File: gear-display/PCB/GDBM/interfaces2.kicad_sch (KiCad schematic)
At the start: 1 part

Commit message: updates
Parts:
- added J?: Con_Screw_1x04_691313510004, KD_Connector_Screw:CON_508_1X04_691313510004_Mated, symbol KD_Connector_Screw:Con_Screw_1x04_691313510004
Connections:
- net +5V: now reaches J?.1 (Pin_1)
- net SDA: now reaches J?.2 (Pin_2)
- net SCL: now reaches J?.3 (Pin_3)
- net GND: now reaches J?.4 (Pin_4)
- net GND: now also J?.4 (Pin_4)
- new net +12V: J?.1 (Pin_1)
- new net PWM: J?.2 (Pin_2)
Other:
- moved on the sheet: J?
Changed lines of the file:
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@@
 (kicad_sch (version 20211123) (generator eeschema)
   (paper "A4")
-  (symbol (lib_id "KD_Connector_Screw:Con_Screw_1x04_691313510004") (at 166.37 53.34 0) (unit 1)
+  (bus_entry (at 163.83 58.42) (size 2.54 2.54)
+    (stroke (width 0) (type default) (color 0 0 0 0))
+  )
+  (bus_entry (at 163.83 60.96) (size 2.54 2.54)
+    (stroke (width 0) (type default) (color 0 0 0 0))
+  )
+  (wire (pts (xy 184.15 58.42) (xy 181.61 58.42))
+    (stroke (width 0) (type default) (color 0 0 0 0))
+  )
+  (bus (pts (xy 163.83 58.42) (xy 163.83 60.96))
+    (stroke (width 0) (type default) (color 0 0 0 0))
+  )
+  (wire (pts (xy 181.61 54.61) (xy 181.61 58.42))
+    (stroke (width 0) (type default) (color 0 0 0 0))
+  )
+  (wire (pts (xy 175.26 92.71) (xy 180.34 92.71))
+    (stroke (width 0) (type default) (color 0 0 0 0))
+  )
+  (wire (pts (xy 163.83 95.25) (xy 180.34 95.25))
+    (stroke (width 0) (type default) (color 0 0 0 0))
+  )
+  (bus (pts (xy 163.83 60.96) (xy 163.83 64.77))
+    (stroke (width 0) (type default) (color 0 0 0 0))
+  )
+  (wire (pts (xy 166.37 63.5) (xy 184.15 63.5))
+    (stroke (width 0) (type default) (color 0 0 0 0))
+  )
+  (wire (pts (xy 180.34 100.33) (xy 175.26 100.33))
+    (stroke (width 0) (type default) (color 0 0 0 0))
+  )
+  (wire (pts (xy 166.37 60.96) (xy 184.15 60.96))
+    (stroke (width 0) (type default) (color 0 0 0 0))
+  )
+  (wire (pts (xy 175.26 100.33) (xy 175.26 104.14))
+    (stroke (width 0) (type default) (color 0 0 0 0))
+  )
+  (wire (pts (xy 175.26 90.17) (xy 175.26 92.71))
+    (stroke (width 0) (type default) (color 0 0 0 0))
+  )
+  (wire (pts (xy 175.26 97.79) (xy 180.34 97.79))
+    (stroke (width 0) (type default) (color 0 0 0 0))
+  )
+  (wire (pts (xy 181.61 66.04) (xy 181.61 68.58))
+    (stroke (width 0) (type default) (color 0 0 0 0))
+  )
+  (bus (pts (xy 163.83 55.88) (xy 163.83 58.42))
+    (stroke (width 0) (type default) (color 0 0 0 0))
+  )
+  (wire (pts (xy 184.15 66.04) (xy 181.61 66.04))
+    (stroke (width 0) (type default) (color 0 0 0 0))
+  )
+  (bus (pts (xy 158.75 55.88) (xy 163.83 55.88))
+    (stroke (width 0) (type default) (color 0 0 0 0))
+  )
+  (label "SCL" (at 167.64 63.5 0)
+    (effects (font (size 1.27 1.27)) (justify left bottom))
+  )
+  (label "SDA" (at 167.64 60.96 0)
+    (effects (font (size 1.27 1.27)) (justify left bottom))
+  )
+  (hierarchical_label "PWM" (shape input) (at 163.83 95.25 180)
+    (effects (font (size 1.27 1.27)) (justify right))
+  )
+  (hierarchical_label "I2C" (shape input) (at 158.75 55.88 180)
+    (effects (font (size 1.27 1.27)) (justify right))
+  )
+  (symbol (lib_id "power:+12V") (at 175.26 90.17 0) (unit 1)
     (in_bom yes) (on_board yes) (fields_autoplaced)
-    (property "Reference" "J?" (id 0) (at 173.99 55.8799 0)
+    (property "Reference" "#PWR?" (id 0) (at 175.26 93.98 0)
+      (effects (font (size 1.27 1.27)) hide)
+    )
+    (property "Value" "+12V" (id 1) (at 175.26 85.09 0))
+    (property "Footprint" "" (id 2) (at 175.26 90.17 0)
+      (effects (font (size 1.27 1.27)) hide)
+    )
+    (property "Datasheet" "" (id 3) (at 175.26 90.17 0)
+      (effects (font (size 1.27 1.27)) hide)
+    )
+    (pin "1")
+  )
+  (symbol (lib_id "power:GND") (at 175.26 104.14 0) (mirror y) (unit 1)
+    (in_bom yes) (on_board yes)
+    (property "Reference" "#PWR?" (id 0) (at 175.26 110.49 0)
+      (effects (font (size 1.27 1.27)) hide)
+    )
+    (property "Value" "GND" (id 1) (at 175.26 107.95 0))
+    (property "Footprint" "" (id 2) (at 175.26 104.14 0)
+      (effects (font (size 1.27 1.27)) hide)
+    )
+    (property "Datasheet" "" (id 3) (at 175.26 104.14 0)
+      (effects (font (size 1.27 1.27)) hide)
+    )
+    (pin "1")
+  )
+  (symbol (lib_id "power:GND") (at 181.61 68.58 0) (mirror y) (unit 1)
+    (in_bom yes) (on_board yes)
+    (property "Reference" "#PWR?" (id 0) (at 181.61 74.93 0)
+      (effects (font (size 1.27 1.27)) hide)
+    )
+    (property "Value" "GND" (id 1) (at 181.61 72.39 0))
+    (property "Footprint" "" (id 2) (at 181.61 68.58 0)
+      (effects (font (size 1.27 1.27)) hide)
+    )
+    (property "Datasheet" "" (id 3) (at 181.61 68.58 0)
+      (effects (font (size 1.27 1.27)) hide)
+    )
+    (pin "1")
+  )
+  (symbol (lib_id "power:+5V") (at 181.61 54.61 0) (unit 1)
+    (in_bom yes) (on_board yes) (fields_autoplaced)
+    (property "Reference" "#PWR?" (id 0) (at 181.61 58.42 0)
+      (effects (font (size 1.27 1.27)) hide)
+    )
+    (property "Value" "+5V" (id 1) (at 181.61 49.53 0))
+    (property "Footprint" "" (id 2) (at 181.61 54.61 0)
+      (effects (font (size 1.27 1.27)) hide)
+    )
+    (property "Datasheet" "" (id 3) (at 181.61 54.61 0)
+      (effects (font (size 1.27 1.27)) hide)
+    )
+    (pin "1")
+  )
+  (symbol (lib_id "KD_Connector_Screw:Con_Screw_1x04_691313510004") (at 180.34 92.71 0) (unit 1)
+    (in_bom yes) (on_board yes) (fields_autoplaced)
+    (property "Reference" "J?" (id 0) (at 187.96 95.2499 0)
       (effects (font (size 1.27 1.27)) (justify left))
     )
-    (property "Value" "Con_Screw_1x04_691313510004" (id 1) (at 153.67 21.59 0)
+    (property "Value" "Con_Screw_1x04_691313510004" (id 1) (at 167.64 60.96 0)
       (effects (font (size 1.27 1.27)) (justify left) hide)
     )
-    (property "Footprint" "KD_Connector_Screw:CON_508_1X04_691313510004_Mated" (id 2) (at 153.67 39.37 0)
+    (property "Footprint" "KD_Connector_Screw:CON_508_1X04_691313510004_Mated" (id 2) (at 167.64 78.74 0)
       (effects (font (size 1.27 1.27)) (justify left) hide)
     )
-    (property "Datasheet" "https://www.we-online.com/katalog/datasheet/6913135100xx.pdf" (id 3) (at 153.67 41.91 0)
+    (property "Datasheet" "https://www.we-online.com/katalog/datasheet/6913135100xx.pdf" (id 3) (at 167.64 81.28 0)
       (effects (font (size 1.27 1.27)) (justify left) hide)
     )
-    (property "Code" "1x04" (id 4) (at 173.99 58.4199 0)
+    (property "Code" "1x04" (id 4) (at 187.96 97.7899 0)
       (effects (font (size 1.27 1.27)) (justify left))
     )
-    (property "Manufacturer" "Würth Elektronik" (id 5) (at 153.67 24.13 0)
+    (property "Manufacturer" "Würth Elektronik" (id 5) (at 167.64 63.5 0)
       (effects (font (size 1.27 1.27)) (justify left) hide)
     )
-    (property "MFG_PartNo" "691313510004" (id 6) (at 153.67 26.67 0)
+    (property "MFG_PartNo" "691313510004" (id 6) (at 167.64 66.04 0)
       (effects (font (size 1.27 1.27)) (justify left) hide)
     )
-    (property "Supplier" "Digi-Key" (id 7) (at 153.67 29.21 0)
+    (property "Supplier" "Digi-Key" (id 7) (at 167.64 68.58 0)
       (effects (font (size 1.27 1.27)) (justify left) hide)
     )
-    (property "Supplier_PartNo" "732-2072-ND" (id 8) (at 153.67 31.75 0)
+    (property "Supplier_PartNo" "732-2072-ND" (id 8) (at 167.64 71.12 0)
       (effects (font (size 1.27 1.27)) (justify left) hide)
     )
-    (property "DNP" "F" (id 9) (at 153.67 34.29 0)
+    (property "DNP" "F" (id 9) (at 167.64 73.66 0)
       (effects (font (size 1.27 1.27)) (justify left) hide)
     )
-    (property "Price" "0.3" (id 10) (at 153.67 36.83 0)
+    (property "Price" "0.3" (id 10) (at 167.64 76.2 0)
       (effects (font (size 1.27 1.27)) (justify left) hide)
     )
+    (pin "1")
+    (pin "2")
+    (pin "3")
+    (pin "4")
+  )
+  (symbol (lib_id "KD_Connector_Screw:Con_Screw_1x04_691313510004") (at 184.15 58.42 0) (unit 1)
+    (in_bom yes) (on_board yes) (fields_autoplaced)
+    (property "Reference" "J?" (id 0) (at 191.77 60.9599 0)
+      (effects (font (size 1.27 1.27)) (justify left))
+    )
+    (property "Value" "Con_Screw_1x04_691313510004" (id 1) (at 171.45 26.67 0)
+      (effects (font (size 1.27 1.27)) (justify left) hide)
+    )
+    (property "Footprint" "KD_Connector_Screw:CON_508_1X04_691313510004_Mated" (id 2) (at 171.45 44.45 0)
+      (effects (font (size 1.27 1.27)) (justify left) hide)
+    )
+    (property "Datasheet" "https://www.we-online.com/katalog/datasheet/6913135100xx.pdf" (id 3) (at 171.45 46.99 0)
+      (effects (font (size 1.27 1.27)) (justify left) hide)
+    )
+    (property "Code" "1x04" (id 4) (at 191.77 63.4999 0)
+      (effects (font (size 1.27 1.27)) (justify left))
+    )
+    (property "Manufacturer" "Würth Elektronik" (id 5) (at 171.45 29.21 0)
+      (effects (font (size 1.27 1.27)) (justify left) hide)
+    )
+    (property "MFG_PartNo" "691313510004" (id 6) (at 171.45 31.75 0)
+      (effects (font (size 1.27 1.27)) (justify left) hide)
+    )
+    (property "Supplier" "Digi-Key" (id 7) (at 171.45 34.29 0)
+      (effects (font (size 1.27 1.27)) (justify left) hide)
+    )
+    (property "Supplier_PartNo" "732-2072-ND" (id 8) (at 171.45 36.83 0)
+      (effects (font (size 1.27 1.27)) (justify left) hide)
+    )
+    (property "DNP" "F" (id 9) (at 171.45 39.37 0)
+      (effects (font (size 1.27 1.27)) (justify left) hide)
+    )
+    (property "Price" "0.3" (id 10) (at 171.45 41.91 0)
+      (effects (font (size 1.27 1.27)) (justify left) hide)
+    )

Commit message: updates
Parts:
- added J?: Con_Screw_1x04_691313510004, KD_Connector_Screw:CON_508_1X04_691313510004_Mated, symbol KD_Connector_Screw:Con_Screw_1x04_691313510004
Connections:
- net PWM_5V: now reaches J?.3 (Pin_3)
- net PWM renamed PWM_12V
- new net GPIO_OUT_1: J?.1 (Pin_1)
- new net GPIO_OUT_2: J?.2 (Pin_2)
- new net GPIO_OUT_3: J?.3 (Pin_3)
- new net GPIO_OUT_4: J?.4 (Pin_4)
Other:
- moved on the sheet: J?

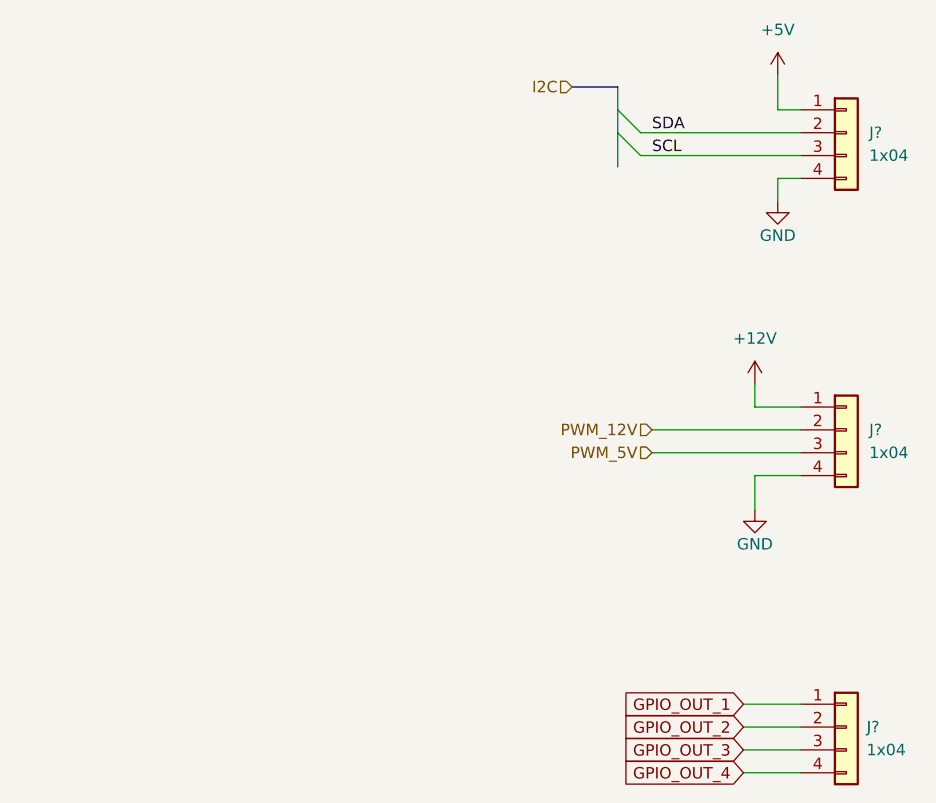
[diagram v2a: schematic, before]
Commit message: changed to match simhub conf
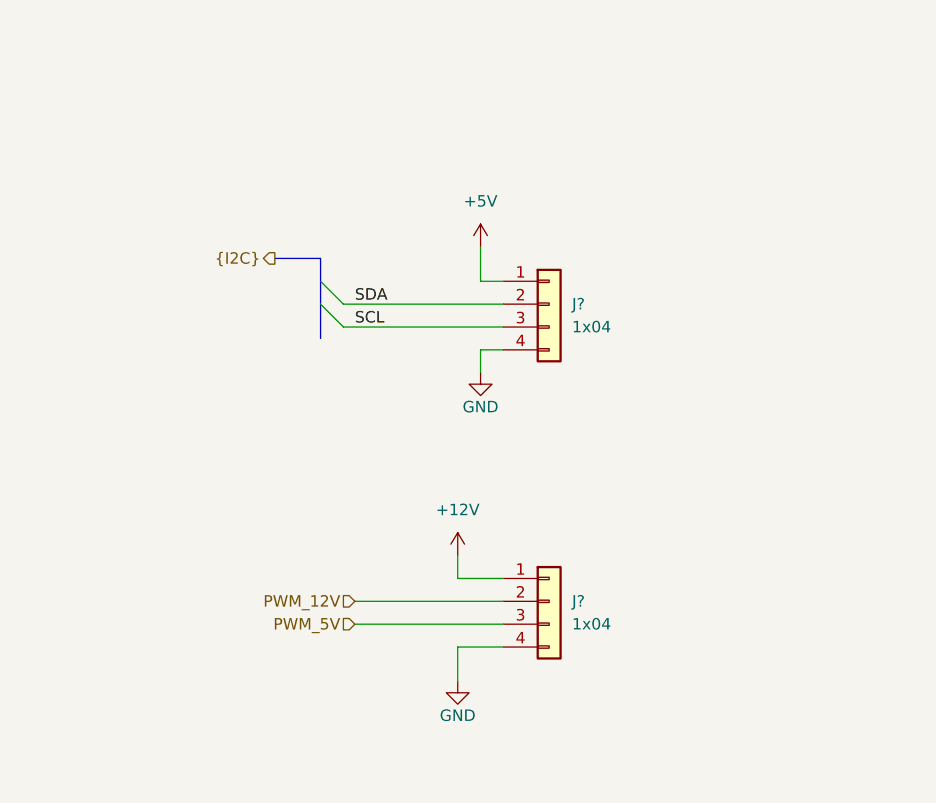
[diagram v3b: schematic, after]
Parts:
- removed J?: Con_Screw_1x04_691313510004, KD_Connector_Screw:CON_508_1X04_691313510004_Mated, symbol KD_Connector_Screw:Con_Screw_1x04_691313510004
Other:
- moved on the sheet: J?

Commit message: rikki
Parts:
- added R31, R32: R_0402_4700_1%, KD_Resistor:RESC1005X40N, symbol KD_Resistor:R_0402_4700_1%
- gave numbers to parts that had none: 2
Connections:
- net +5V: now also R31.1, R32.1
- net SCL: now also R32.2
- net SDA: now also R31.2
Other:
- company: (none) -> Kallio Designs Oy
- title: (none) -> Gear Display Board

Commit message: PSU and LED powering changed
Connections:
- net PWM_12V: now also J7.3 (Pin_3); no longer J7.2 (Pin_2)
- net PWM_5V: now also J7.2 (Pin_2); no longer J7.3 (Pin_3)
- net SCL: now also J6.2 (Pin_2), R31.2; no longer J6.3 (Pin_3), R32.2
- net SDA: now also J6.3 (Pin_3), R32.2; no longer J6.2 (Pin_2), R31.2
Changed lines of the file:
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@@
-    (stroke (width 0) (type default) (color 0 0 0 0))
-  )
-  (wire (pts (xy 134.62 115.57) (xy 151.13 115.57))
     (stroke (width 0) (type default) (color 0 0 0 0))
   )
@@
     (stroke (width 0) (type default) (color 0 0 0 0))
   )
-  (wire (pts (xy 134.62 113.03) (xy 151.13 113.03))
+  (wire (pts (xy 134.62 115.57) (xy 151.13 115.57))
     (stroke (width 0) (type default) (color 0 0 0 0))
   )
@@
     (stroke (width 0) (type default) (color 0 0 0 0))
   )
+  (wire (pts (xy 134.62 113.03) (xy 151.13 113.03))
+    (stroke (width 0) (type default) (color 0 0 0 0))
+  )
   (wire (pts (xy 124.46 76.2) (xy 124.46 80.01))
     (stroke (width 0) (type default) (color 0 0 0 0))
@@
     (stroke (width 0) (type default) (color 0 0 0 0))
   )
-  (label "SCL" (at 114.3 82.55 0)
+  (label "SDA" (at 114.3 82.55 0)
     (effects (font (size 1.27 1.27)) (justify left bottom))
   )
-  (label "SDA" (at 114.3 80.01 0)
+  (label "SCL" (at 114.3 80.01 0)
     (effects (font (size 1.27 1.27)) (justify left bottom))
   )
-  (hierarchical_label "PWM_5V" (shape input) (at 134.62 115.57 180)
+  (hierarchical_label "PWM_5V" (shape input) (at 134.62 113.03 180)
     (effects (font (size 1.27 1.27)) (justify right))
   )
-  (hierarchical_label "PWM_12V" (shape input) (at 134.62 113.03 180)
+  (hierarchical_label "PWM_12V" (shape input) (at 134.62 115.57 180)
     (effects (font (size 1.27 1.27)) (justify right))
   )
